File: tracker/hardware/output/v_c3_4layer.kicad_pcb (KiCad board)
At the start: 4 copper layers, 35 x 30 mm, 17 parts, among them U1 ESP32-C3, U2 LR2021F33, U3 MAX-M10S, U4 TPS7A02

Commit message: feat: C3 flight PCB — 20 footprints, 41 tracks, 4-layer, 0.6mm (DRC needs fixing)
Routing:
- net LR2021_DIO9: track 33.5 -> 0.00 mm
- net LR2021_RST: track 33.2 -> 0.00 mm
- net VDIV_MID: track 8.86 -> 31.4 mm, vias 0 -> 2
- net VCAP: track 0.00 -> 7.47 mm
- net SPI_NSS: track 0.00 -> 4.91 mm
- net RF_SUB_868: track 35.9 -> 37.9 mm, vias 0 -> 2
- net GND: vias 0 -> 21
- net 3V3: vias 0 -> 7

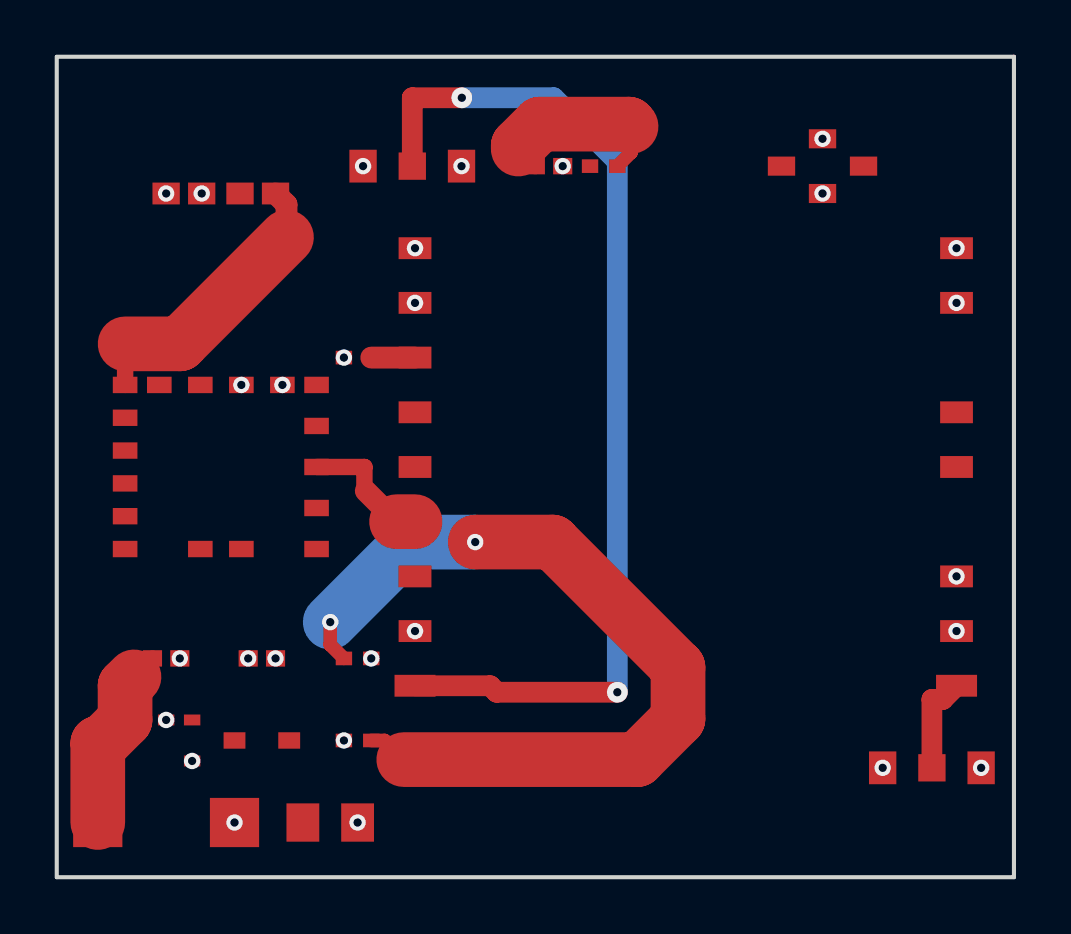
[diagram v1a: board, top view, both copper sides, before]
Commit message: feat: C3 flight PCB — collision-aware routing (80 tracks, 26 vias), real gerbers exported
Board: 20 footprints, 80 tracks, 26 vias, 4 layers, 0.6mm
DRC: 325 violations (247 cosmetic silk, 56 real — placement overlap + duplicate pads)
Gerbers: F_Cu=13.6KB, In1(GND)=35KB, In2(3V3)=35KB

Remaining issues:
- 13 shorting_items: U1 pad 19 duplicate, U2/ANT1 placement overlap
- 22 unconnected: nets that couldn't route around obstacles
- 12 drill_out_of_range: via drill size

Router: c3_router.py (collision-aware, K2.7-written)
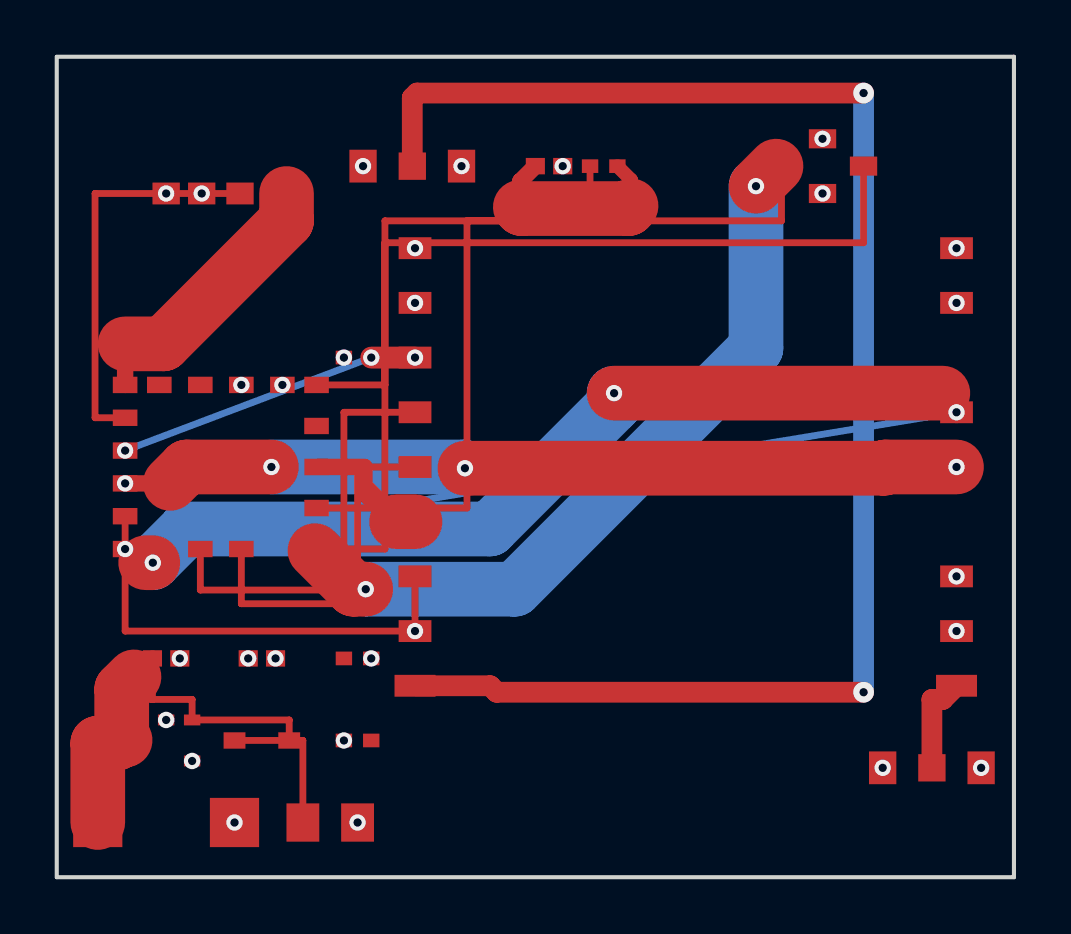
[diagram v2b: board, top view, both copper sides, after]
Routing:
- net LR2021_DIO9: track 0.00 -> 64.6 mm, vias 0 -> 4
- net LR2021_RST: track 0.00 -> 61.1 mm, vias 0 -> 4
- net FEM_TX: track 0.00 -> 58.6 mm, vias 0 -> 2
- net VDIV_MID: track 31.4 -> 0.00 mm, vias 2 -> 0
- net FEM_RX: track 0.00 -> 28.0 mm
- net LED: track 0.00 -> 22.5 mm
- net RF_SUB_868: track 37.9 -> 57.5 mm
- net LR2021_BUSY: track 0.00 -> 16.8 mm
- net SPI_MOSI: track 0.00 -> 15.3 mm
- net GPS_RX: track 0.00 -> 14.6 mm
- net SPI_SCK: track 0.00 -> 13.8 mm
- net SPI_MISO: track 1.60 -> 12.8 mm, vias 0 -> 3
- net 3V3: track 0.00 -> 8.35 mm
- net VCAP: track 7.47 -> 14.5 mm
- net SOLAR_IN: track 0.00 -> 5.50 mm

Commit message: docs: add Gate 0 placement check before routing — no component overlap allowed
Quality gate added after v1 had 13 shorting items from overlapping footprints.
Components must have 2mm gap. Placement verified BEFORE any routing begins.
Task t_e1cb2d49 dispatched to worker-layout (Kimi K2.7).
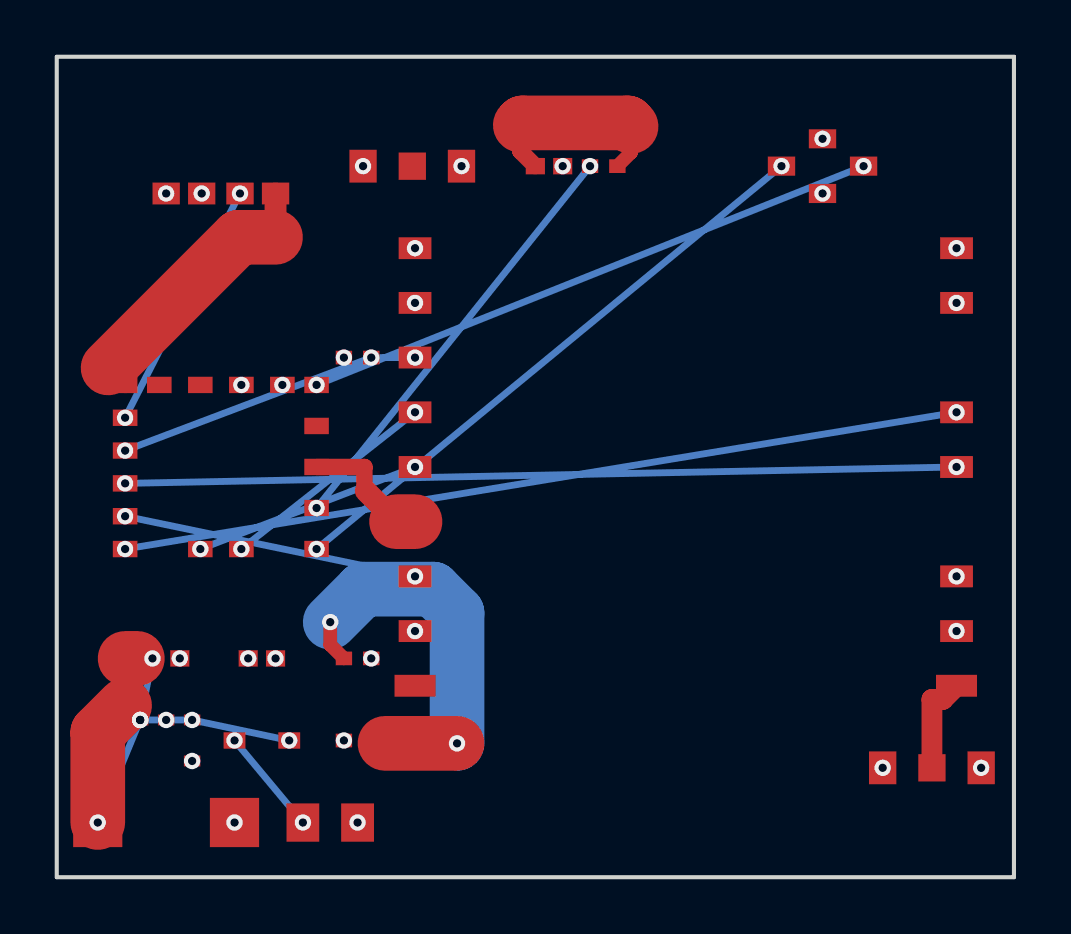
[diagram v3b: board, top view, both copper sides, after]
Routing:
- net RF_SUB_868: track 57.5 -> 0.00 mm, vias 2 -> 0
- net FEM_TX: track 58.6 -> 22.0 mm
- net LR2021_DIO9: track 64.6 -> 30.8 mm, vias 4 -> 2
- net LR2021_RST: track 61.1 -> 30.4 mm, vias 4 -> 2
- net VDIV_MID: track 0.00 -> 15.0 mm, vias 0 -> 2
- net SPI_MOSI: track 15.3 -> 8.08 mm, vias 0 -> 2
- net LED: track 22.5 -> 16.0 mm, vias 0 -> 2
- net FEM_RX: track 28.0 -> 21.5 mm, vias 0 -> 2
- net LR2021_BUSY: track 16.8 -> 10.8 mm, vias 0 -> 2
- net SPI_SCK: track 13.8 -> 8.40 mm, vias 0 -> 2
- net GPS_RX: track 14.6 -> 9.21 mm, vias 0 -> 2
- net VCAP: track 14.5 -> 11.9 mm, vias 0 -> 6
- net SPI_MISO: track 12.8 -> 11.2 mm
- net SOLAR_IN: track 5.50 -> 3.91 mm, vias 0 -> 2
- net 3V3: track 8.35 -> 8.95 mm
